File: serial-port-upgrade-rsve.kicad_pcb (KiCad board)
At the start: 4 copper layers, 35.6 x 43.2 mm, 20 parts, among them J1 MFP RC, J2 MFP TDO, J3 VCC, J4 GND, J5 Led, J6 IDC connector, U1 GAL16V8_PHY, U2 12-STAGE_BINARY_RIPPLE_COUNTE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, X1 1,8432 MHz

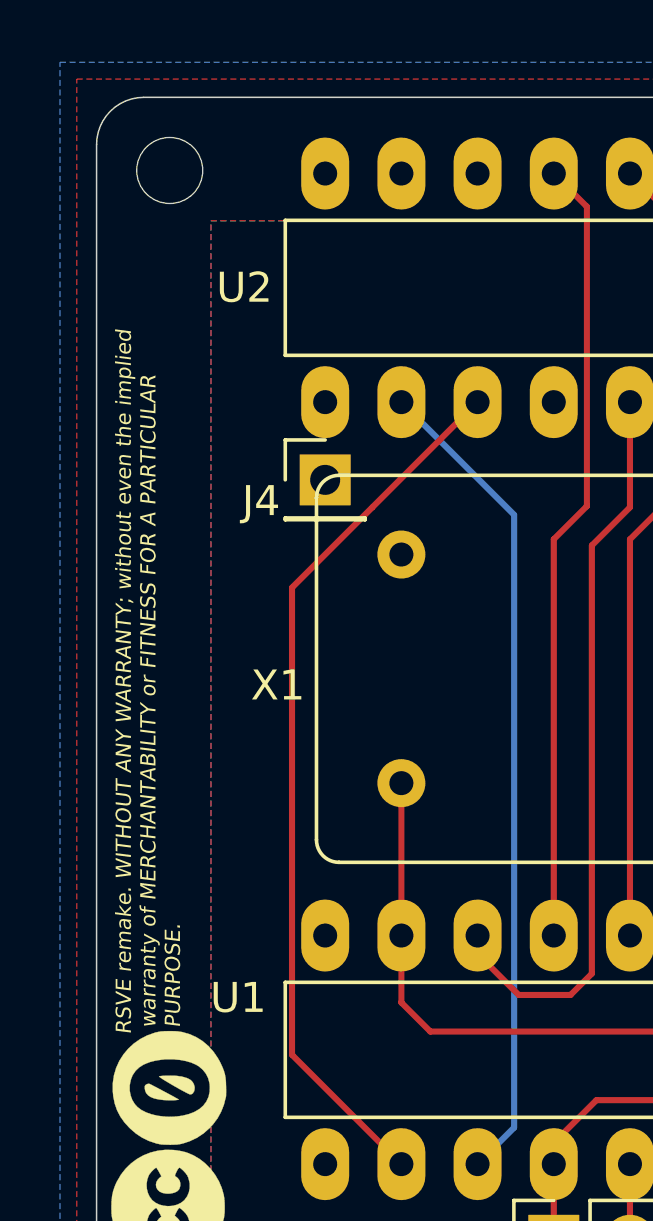
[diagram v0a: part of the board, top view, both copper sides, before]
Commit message: notice/disclaimer sizing
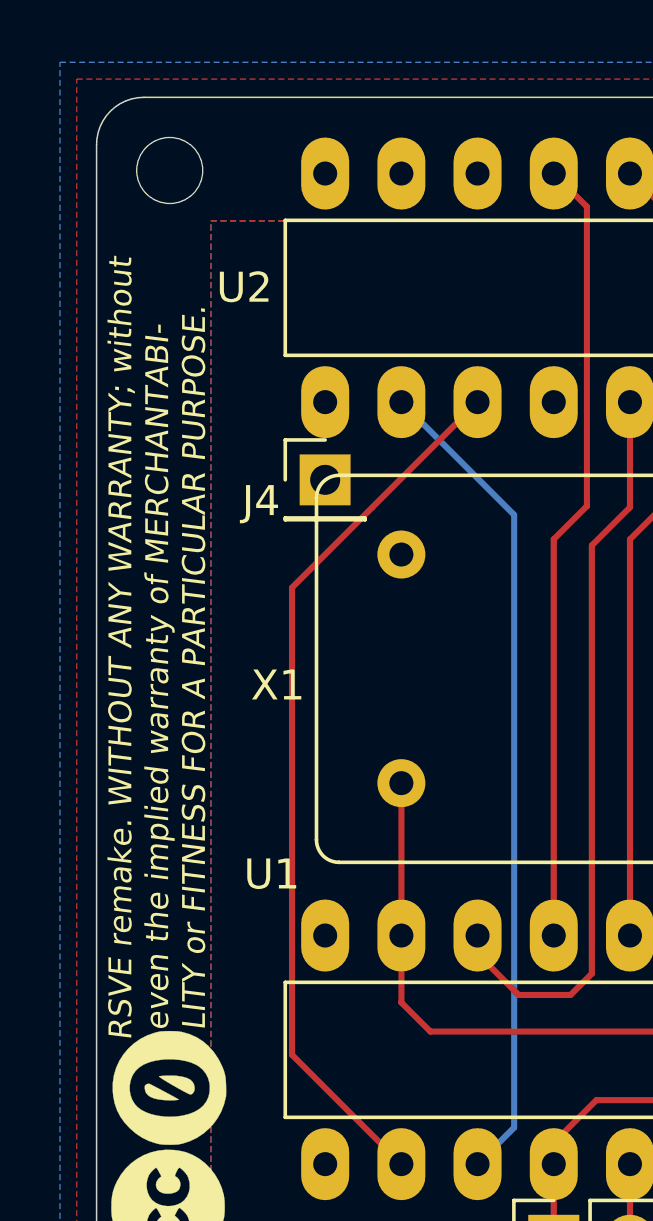
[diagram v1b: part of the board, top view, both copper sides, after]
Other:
- board text added: "RSVE remake. WITHOUT ANY WARRANTY; without even the implied warranty of MERCHANTABI- LITY or FITNESS FOR A PARTICULAR PURPOSE."
- board text removed: "RSVE remake. WITHOUT ANY WARRANTY; without even the implied warranty of MERCHANTABILITY or FITNESS FOR A PARTICULAR PURPOSE."
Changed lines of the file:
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@@
     (descr "20-lead though-hole mounted DIP package, row spacing 7.62 mm (300 mils), LongPads")
     (tags "THT DIP DIL PDIP 2.54mm 7.62mm 300mil LongPads")
-    (fp_text reference U1 (at 2.0828 25.7556 180) (layer F.SilkS)
+    (fp_text reference U1 (at -2.032 24.638 180) (layer F.SilkS)
       (effects (font (size 1 1) (thickness 0.15)))
     )
@@
     (effects (font (size 0.762 0.762) (thickness 0.1016)) (justify mirror))
   )
-  (gr_text "RSVE remake. WITHOUT ANY WARRANTY; without even the implied\n warranty of MERCHANTABILITY or FITNESS FOR A PARTICULAR\n PURPOSE." (at 77.9272 107.3912 90) (layer F.SilkS)
-    (effects (font (size 0.508 0.508) (thickness 0.1016) italic) (justify left))
+  (gr_text "RSVE remake. WITHOUT ANY WARRANTY; without\n even the implied warranty of MERCHANTABI-\n LITY or FITNESS FOR A PARTICULAR PURPOSE." (at 78.232 107.5944 90) (layer F.SilkS)
+    (effects (font (size 0.762 0.762) (thickness 0.127) italic) (justify left))
   )
   (gr_line (start 109.6772 88.9) (end 109.6772 88.6968) (layer F.SilkS) (width 0.12))
